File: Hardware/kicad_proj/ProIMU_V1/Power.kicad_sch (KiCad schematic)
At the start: 7 parts, among them SW1 SW_SPDT, U7 TPS54308

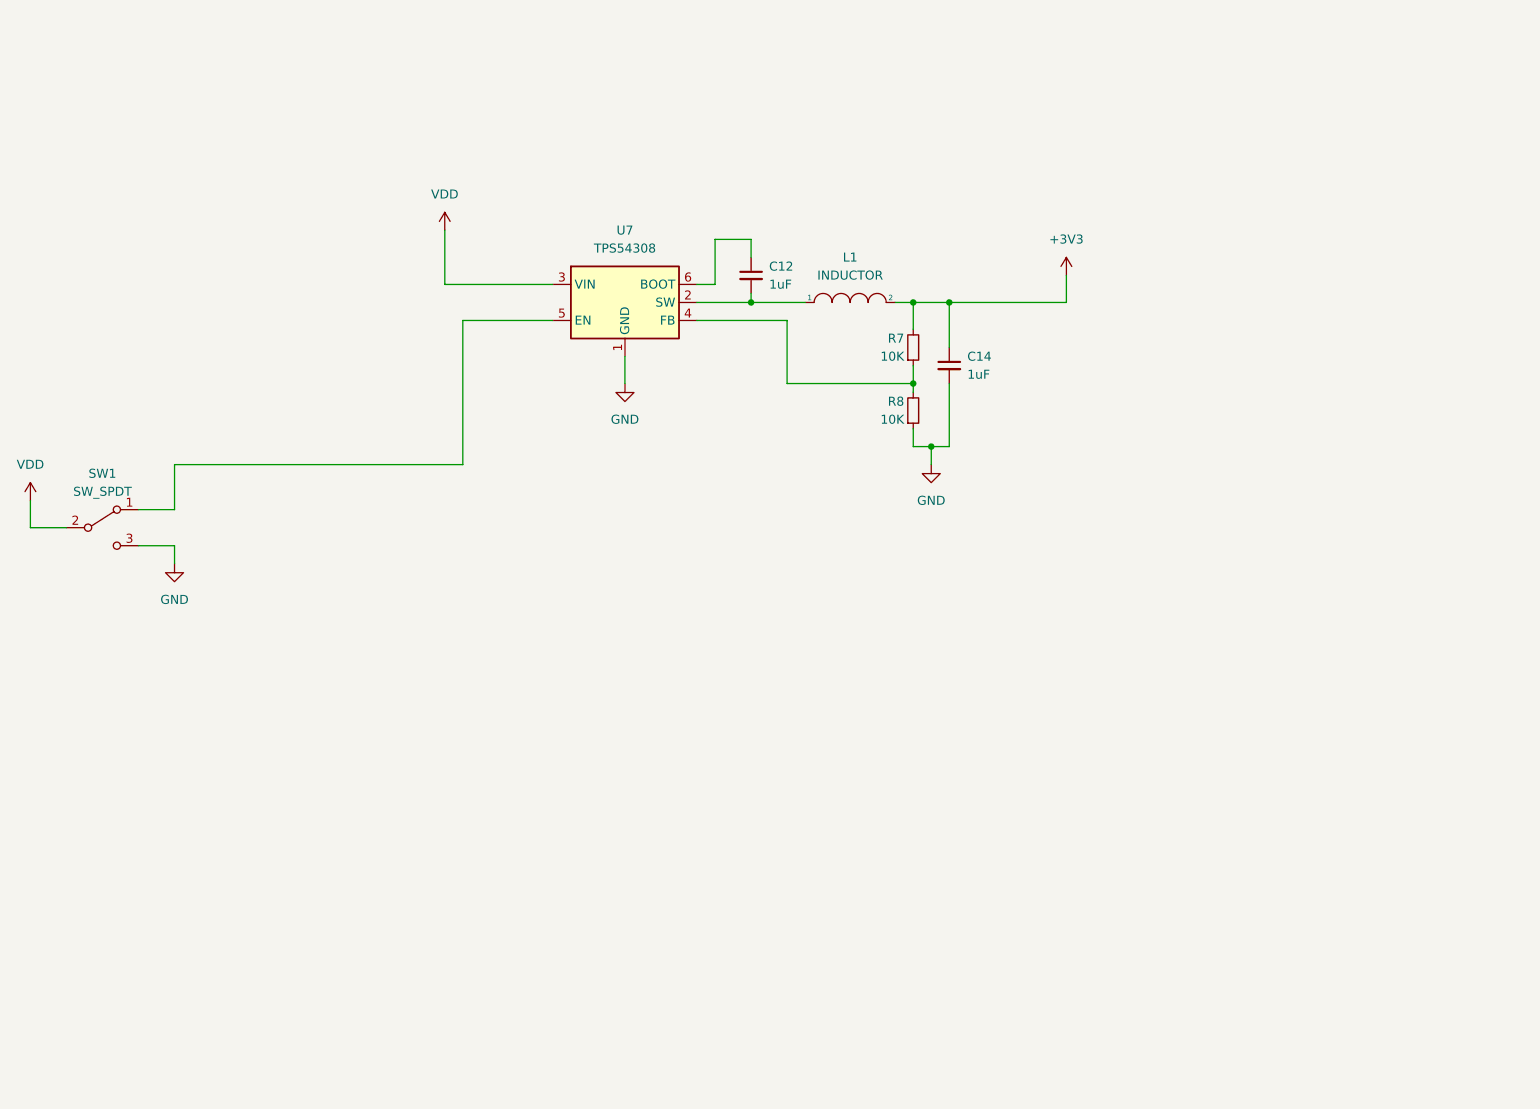
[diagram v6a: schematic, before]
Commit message: Updated schematic and removed redundant schematic
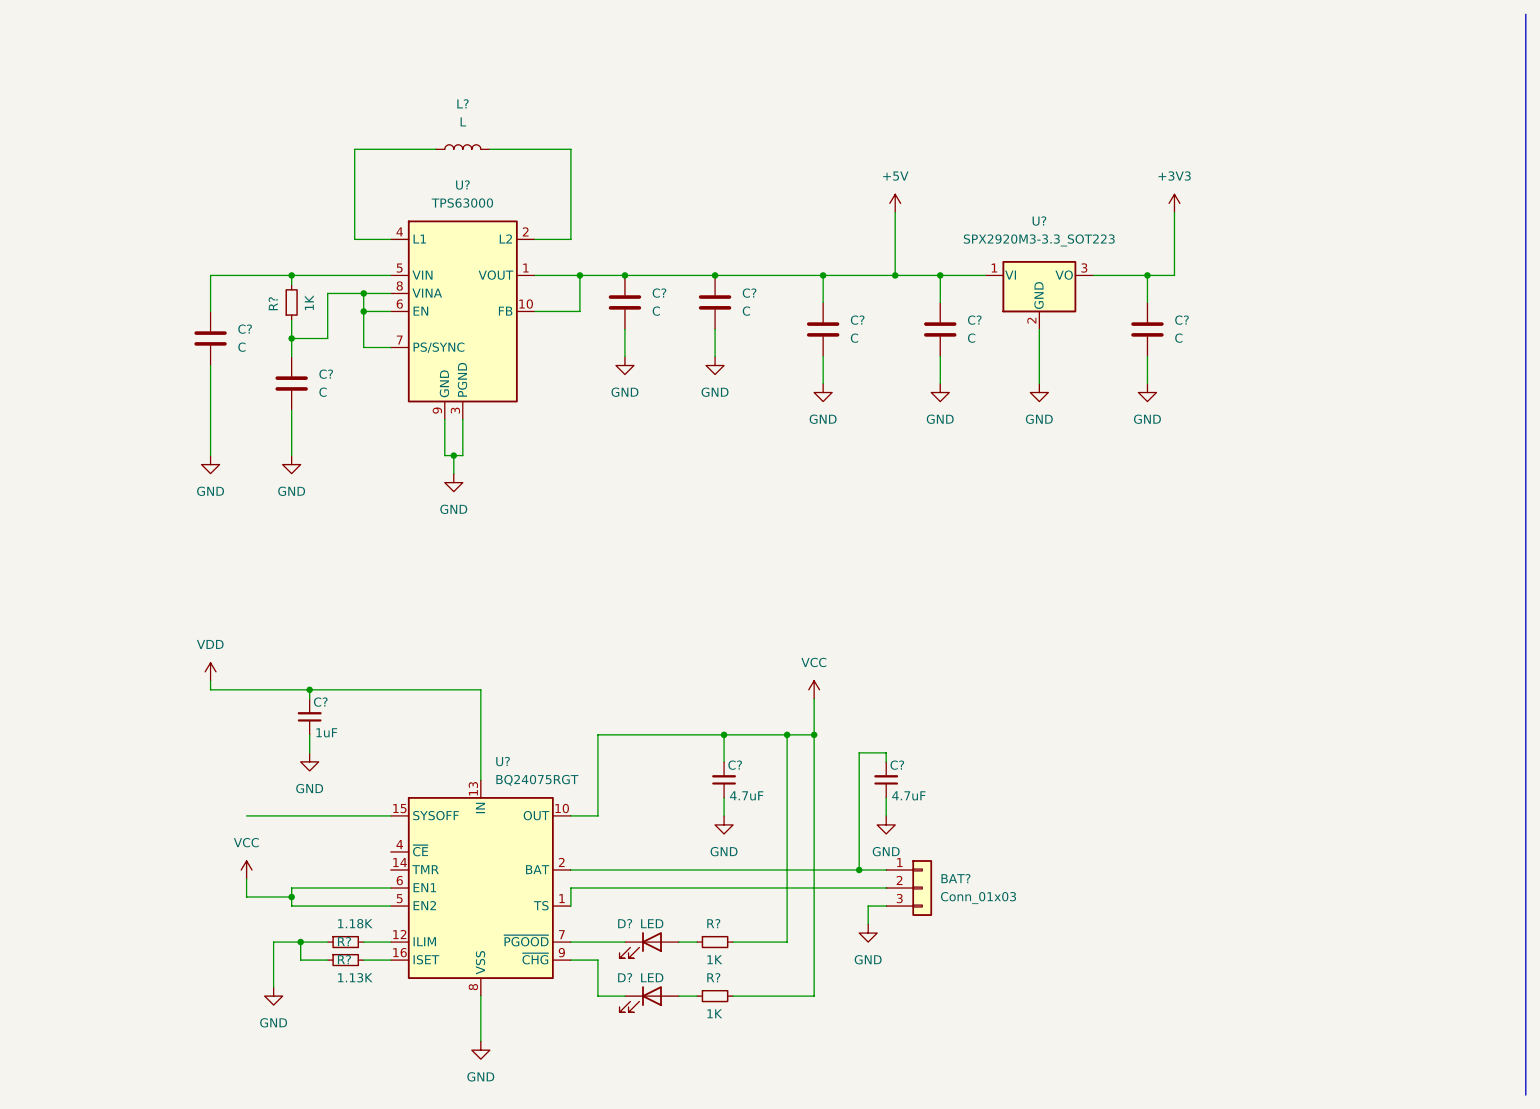
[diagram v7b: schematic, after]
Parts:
- removed C12, C14: 1uF, Capacitor_SMD:C_0402_1005Metric_Pad0.74x0.62mm_HandSolder, symbol Device:C_Small
- removed L1: INDUCTOR, symbol pspice:INDUCTOR
- removed R7, R8: 10K, Resistor_SMD:R_0402_1005Metric_Pad0.72x0.64mm_HandSolder, symbol Device:R_Small
- removed SW1: SW_SPDT, symbol Switch:SW_SPDT
- removed U7: TPS54308, Package_TO_SOT_SMD:SOT-23-6, symbol Regulator_Switching:TPS54308
- added BAT?: Conn_01x03, symbol Connector_Generic:Conn_01x03
- added C? (x7): C, Capacitor_SMD:C_0805_2012Metric_Pad1.18x1.45mm_HandSolder, symbol Device:C
- added C? (x2): 4.7uF, Capacitor_SMD:C_0402_1005Metric_Pad0.74x0.62mm_HandSolder, symbol Device:C_Small
- added C?: 1uF, Capacitor_SMD:C_0402_1005Metric_Pad0.74x0.62mm_HandSolder, symbol Device:C_Small
- added D? (x2): LED, symbol Device:LED
- added L?: L, symbol Device:L
- added R?: 1.18K, Resistor_SMD:R_0402_1005Metric_Pad0.72x0.64mm_HandSolder, symbol Device:R_Small
- added R? (x3): 1K, Resistor_SMD:R_0402_1005Metric_Pad0.72x0.64mm_HandSolder, symbol Device:R_Small
- added R?: 1.13K, Resistor_SMD:R_0402_1005Metric_Pad0.72x0.64mm_HandSolder, symbol Device:R_Small
- added U?: SPX2920M3-3.3_SOT223, Package_TO_SOT_SMD:SOT-223-3_TabPin2, symbol Regulator_Linear:SPX2920M3-3.3_SOT223
- added U?: BQ24075RGT, Package_DFN_QFN:VQFN-16-1EP_3x3mm_P0.5mm_EP1.6x1.6mm, symbol Battery_Management:BQ24075RGT
- added U?: TPS63000, Package_SON:Texas_DRC0010J_ThermalVias, symbol Regulator_Switching:TPS63000
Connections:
- net +3V3: now also C?.1, U?.3 (VO)
- net GND: now also BAT?.3 (Pin_3), C?.1, C?.1, C?.1, C?.2, C?.2, C?.2, C?.2, C?.2, C?.2, C?.2, R?.1, R?.1, U?.11 (PGND), U?.17 (VSS), U?.2 (GND), U?.3 (PGND), U?.8 (VSS), U?.9 (GND)
- net VDD: now also C?.2, U?.13 (IN)
- new net: C?.1, R?.1, U?.6 (EN), U?.7 (PS/SYNC), U?.8 (VINA)
- new net: BAT?.2 (Pin_2), U?.1 (TS)
- new net: R?.2, U?.12 (ILIM)
- new net: R?.2, U?.16 (ISET)
- new net: BAT?.1 (Pin_1), C?.2, U?.2 (BAT), U?.3 (BAT)
- new net: D?.1 (K), U?.7 (~{PGOOD})
- new net: D?.1 (K), U?.9 (~{CHG})
- new net: C?.1, R?.2, U?.5 (VIN)
- new net: L?.1, U?.4 (L1)
- new net: L?.2, U?.2 (L2)
- new net: D?.2 (A), R?.1 (x2)
- new net +5V: C?.1, C?.1, C?.1, C?.1, U?.1 (VI), U?.1 (VOUT), U?.10 (FB)
- new net VCC: C?.2, R?.2, R?.2, U?.10 (OUT), U?.11 (OUT), U?.5 (EN2), U?.6 (EN1)

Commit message: Updated Schematic and Layout
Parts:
- gave numbers to parts that had none: 22
